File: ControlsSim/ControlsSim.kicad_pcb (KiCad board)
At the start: 2 copper layers, 100 x 100 mm, 22 parts, among them J10 DisplayConn, J2 Accel_Pots, J3 Brake_Pots, J5 Motor Contactors, J6 Array Contactors, J7 Conn_01x14, J8 Minion Passthrough In, J9 Minion Passthrough Out, SW2 SW_Rotary2x6

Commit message: almost final PCB
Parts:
- removed RV2: Brake_Pot1, Footprints:PTA4543
- removed RV3: Accel_Pot2, Footprints:PTA4543
- removed RV4: Brake_Pot2, Footprints:PTA4543
- added H2: MountingHole, MountingHole:MountingHole_3.2mm_M3, F.Cu at (196.0, 54.0)
- added H3: MountingHole, MountingHole:MountingHole_3.2mm_M3, F.Cu at (196.0, 146.0)
- added R5: 10k, Resistor_SMD:R_0805_2012Metric, B.Cu at (174.0, 140.0)
- added S1: Brake, Footprints:TS16121295BK260SMTTR, F.Cu at (174.5, 142.5)
- J10: value DisplayConn -> Display
- J2: value Accel_Pots -> Accelerator Pot
- J3: value Brake_Pots -> Brake Button
- J7: value Conn_01x14 -> Rotary Switch
- R1, R2, R3, R4: moved to B.Cu
- RV1: value Accel_Pot1 -> Accelerator
- moved J5 75.0 mm to (112.5, 73.1)
- moved J6 57.2 mm to (112.5, 92.6)
- moved D1 54.3 mm to (111.0, 136.0)
- moved D2 54.3 mm to (111.0, 139.0)
- moved R2 54.2 mm to (118.5, 139.0)
- moved R1 53.9 mm to (118.5, 136.0)
- moved R4 24.3 mm to (148.0, 136.0)
- moved D3 24.0 mm to (140.5, 139.0)
- moved D4 24.0 mm to (140.5, 136.0)
- moved R3 24.0 mm to (148.0, 139.0)
- moved SW2 21.9 mm to (153.5, 103.5), turned to 180 degrees
- moved RV1 8.02 mm to (192.0, 108.5)
- moved J2 6.01 mm to (193.0, 71.5)
- moved J7 3.00 mm to (172.5, 57.5)
- moved J8 3.00 mm to (126.5, 57.5)
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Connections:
- net /Acc_Pot1_Gnd renamed /Acc_Pot_Gnd
- net /Acc_Pot1_V+ renamed /Acc_Pot_V+
- net /Acc_Pot1_Vo renamed /Acc_Pot_Vo
- J2 pad 4: /Acc_Pot2_V+ -> unconnected-(J2-Pad4)
- J2 pad 5: /Acc_Pot2_Vo -> unconnected-(J2-Pad5)
- J2 pad 6: /Acc_Pot2_Gnd -> unconnected-(J2-Pad6)
- J3 pad 1: /Brk_Pot1_V+ -> /Brk_V+
- J3 pad 2: /Brk_Pot1_Vo -> /Brk_Signal
- J3 pad 3: /Brk_Pot1_Gnd -> /Brk_GND
- J3 pad 4: /Brk_Pot2_V+ -> unconnected-(J3-Pad4)
- J3 pad 5: /Brk_Pot2_Vo -> unconnected-(J3-Pad5)
- J3 pad 6: /Brk_Pot2_Gnd -> unconnected-(J3-Pad6)
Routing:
- net +5V: track 0.00 -> 165.8 mm
- net GND: track 0.00 -> 114.6 mm
- net /Brk_Signal: track 0.00 -> 104.2 mm, vias 0 -> 1
- net /Brk_GND: track 0.00 -> 84.9 mm, vias 0 -> 1
- net /Brk_V+: track 0.00 -> 84.7 mm
- net /M_D_Pre2: track 0.00 -> 81.1 mm
- net /Rot8: track 0.00 -> 79.1 mm
- net /Acc_Pot_Gnd: track 0.00 -> 78.0 mm
- net /M_D_Mn2: track 0.00 -> 76.3 mm
- net /Rot7: track 0.00 -> 73.0 mm
- net /A_D_Mn2: track 0.00 -> 72.4 mm
- net /Rot9: track 0.00 -> 70.3 mm
- net /Rot5: track 0.00 -> 65.3 mm
- net /RotV+: track 0.00 -> 62.9 mm
- net /A_D_Pre2: track 0.00 -> 61.9 mm
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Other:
- outline, holes or cut-outs redrawn
- board text added: "5V"
- board text added: "Array Main Contactor"
- board text added: "Array Precharge Contactor"
- board text added: "Controls Simulation Board"
- board text added: "Fast ____ Slow"
- board text added: "Gnd"
- board text added: "Longhorn Racing Solar 2022-2023"
- board text added: "Motor Main Contactor"
- board text added: "Rx"
- board text added: "Tx"

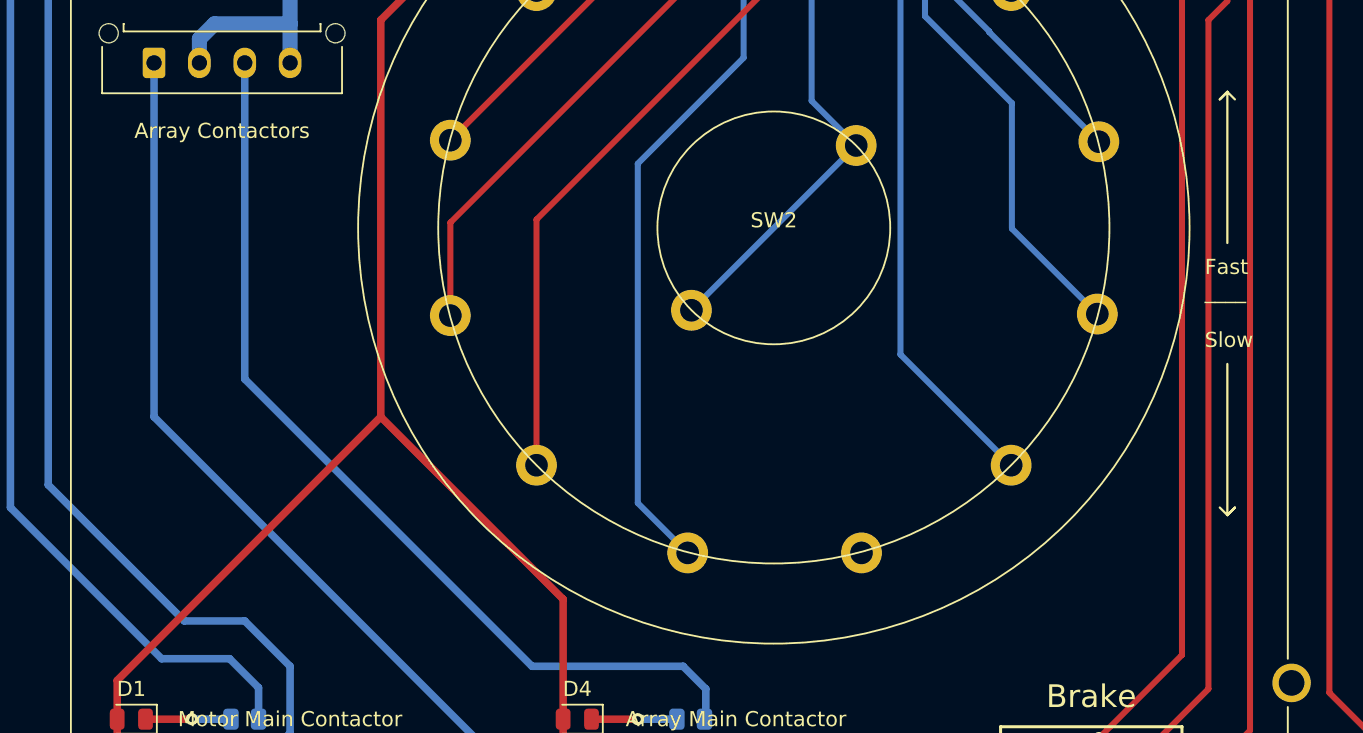
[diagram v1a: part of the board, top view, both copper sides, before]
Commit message: added logos
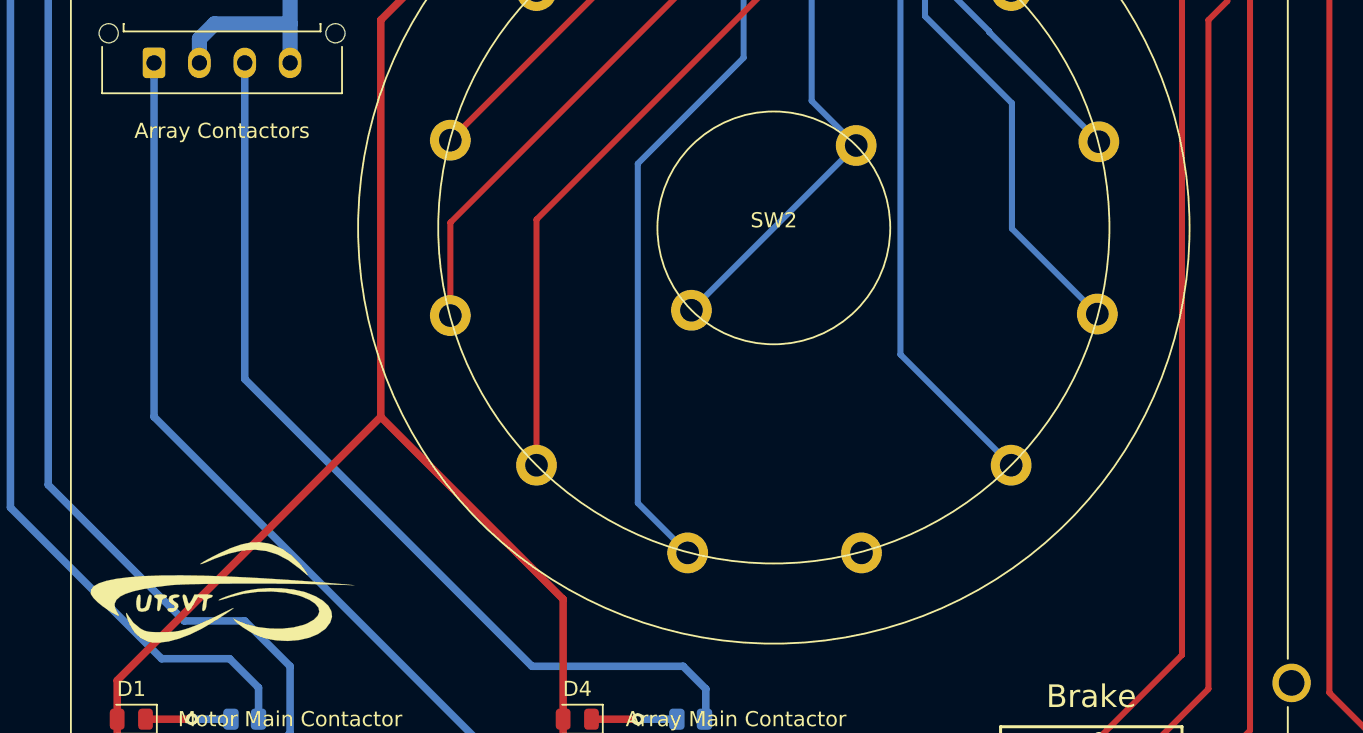
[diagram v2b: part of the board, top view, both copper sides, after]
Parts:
- added LOGO1: Hallock, UTSVT_Special:Hallock_Image_Small, B.Cu at (149.0, 98.0)
- added LOGO2: UTSVT Logo, UTSVT_Special:UTSVT_Logo_Symbol, F.Cu at (116.8, 127.8)
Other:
- board text added: "Alex Zhang"
- board text added: "Jacob Pustilnik Lauren Oliveira Aditi Sarlashkar"
- board text removed: "Fast ____ Slow"

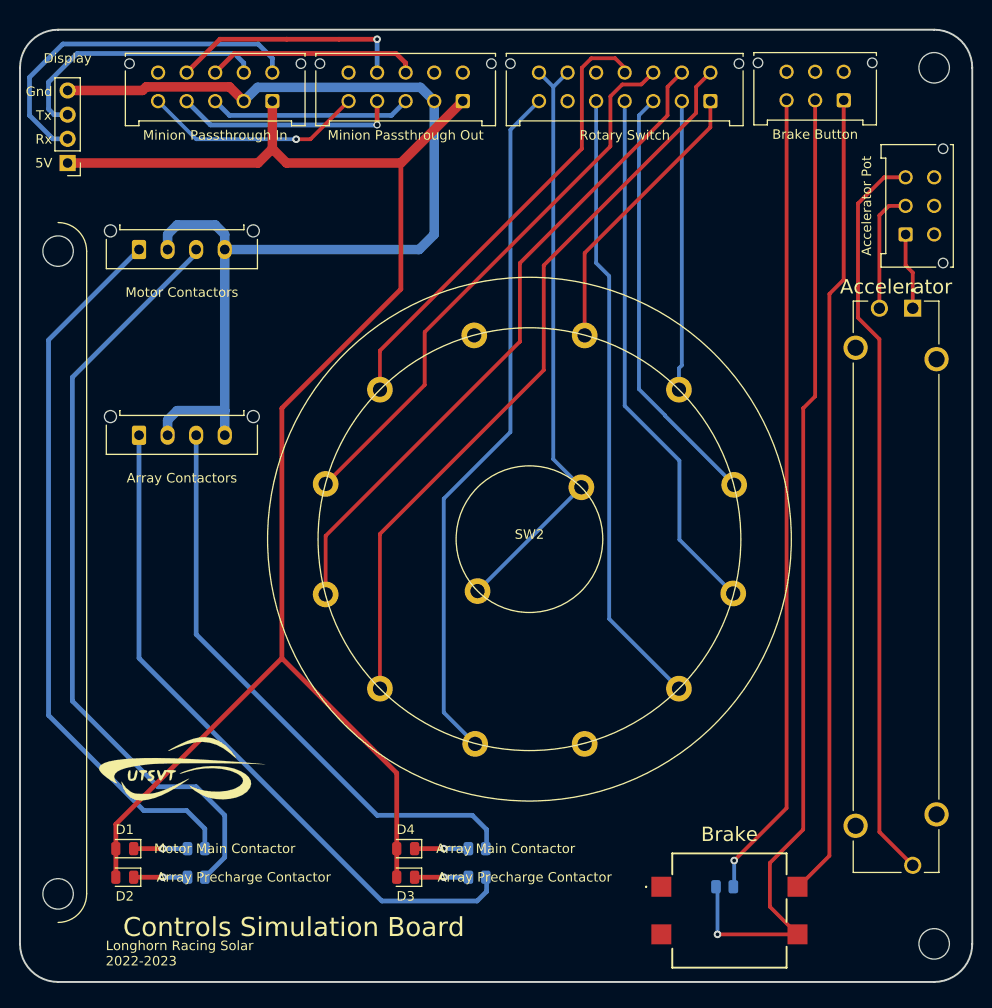
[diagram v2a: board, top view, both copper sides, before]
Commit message: removed display connector
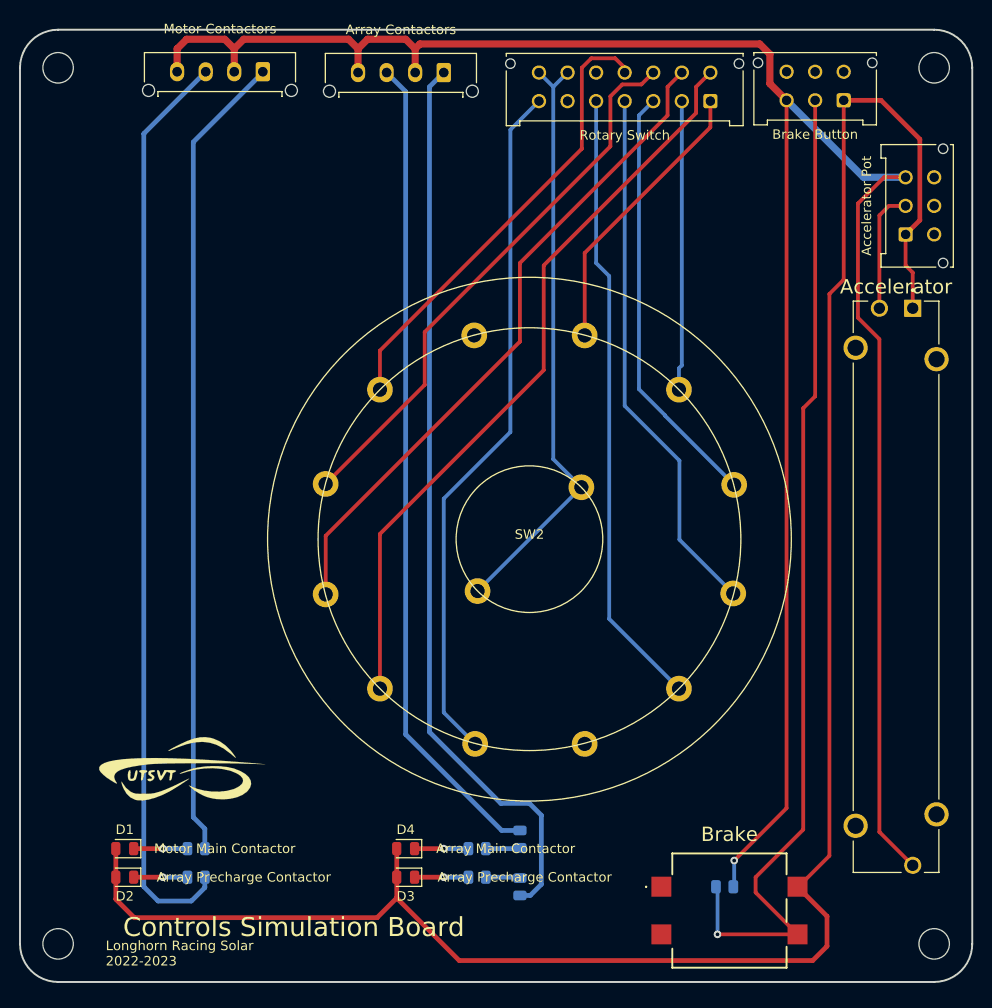
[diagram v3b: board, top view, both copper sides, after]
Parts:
- removed J10: Display, Connector_PinHeader_2.54mm:PinHeader_1x04_P2.54mm_Vertical
- removed J8: Minion Passthrough In, Connector_Molex:Molex_Micro-Fit_3.0_43045-1012_2x05_P3.00mm_Vertical
- removed J9: Minion Passthrough Out, Connector_Molex:Molex_Micro-Fit_3.0_43045-1012_2x05_P3.00mm_Vertical
- added H4: MountingHole, MountingHole:MountingHole_3.2mm_M3, F.Cu at (104.0, 54.0)
- added R6: 330, Resistor_SMD:R_0805_2012Metric, B.Cu at (152.5, 140.0)
- added R7: 330, Resistor_SMD:R_0805_2012Metric, B.Cu at (152.5, 135.0)
- H1: value Display Mounting Holes -> MountingHole
- R1, R2: value 1k -> 330
- R3, R4: value 1.5k -> 330
- moved H1 72.8 mm to (104.0, 146.0)
- moved J6 49.7 mm to (144.5, 54.5), turned to 180 degrees
- moved J5 22.8 mm to (125.5, 54.4), turned to 180 degrees
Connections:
- D1 pad 2: +5V -> +3V3
- D2 pad 2: +5V -> +3V3
- D3 pad 2: +5V -> +3V3
- D4 pad 2: +5V -> +3V3
- J2 pad 1: /Acc_Pot_V+ -> +3V3
- J2 pad 3: /Acc_Pot_Gnd -> GND
- J3 pad 1: /Brk_V+ -> +3V3
- J3 pad 3: /Brk_GND -> GND
- R3 pad 2: /A_D_Mn2 -> /X1
- R4 pad 2: /A_D_Pre2 -> /X2
- R5 pad 2: /Brk_GND -> GND
- RV1 pad 1: /Acc_Pot_V+ -> +3V3
- RV1 pad 3: /Acc_Pot_Gnd -> GND
- S1 pad 2: /Brk_V+ -> +3V3
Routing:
- net +3V3: track 0.00 -> 210.7 mm
- net +5V: track 165.8 -> 0.00 mm
- net GND: track 114.6 -> 259.6 mm, vias 0 -> 1
- net /Brk_GND: track 84.9 -> 0.00 mm, vias 1 -> 0
- net /Brk_V+: track 84.7 -> 0.00 mm
- net /Acc_Pot_Gnd: track 78.0 -> 0.00 mm
- net /UART_Tx: track 38.1 -> 0.00 mm
- net /UART_Rx: track 28.2 -> 0.00 mm
- net /CS: track 24.9 -> 0.00 mm, vias 1 -> 0
- net /A_D_Pre2: track 61.9 -> 86.5 mm
- net /MISO: track 23.5 -> 0.00 mm, vias 1 -> 0
- net /BPS_PWR: track 23.3 -> 0.00 mm, vias 1 -> 0
- net /A_D_Mn2: track 72.4 -> 95.2 mm
- net /CLK: track 22.2 -> 0.00 mm
- net /MOSI: track 21.2 -> 0.00 mm
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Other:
- board text removed: "5V"
- board text removed: "Gnd"
- board text removed: "Rx"
- board text removed: "Tx"
